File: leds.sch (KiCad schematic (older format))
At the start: 36 parts

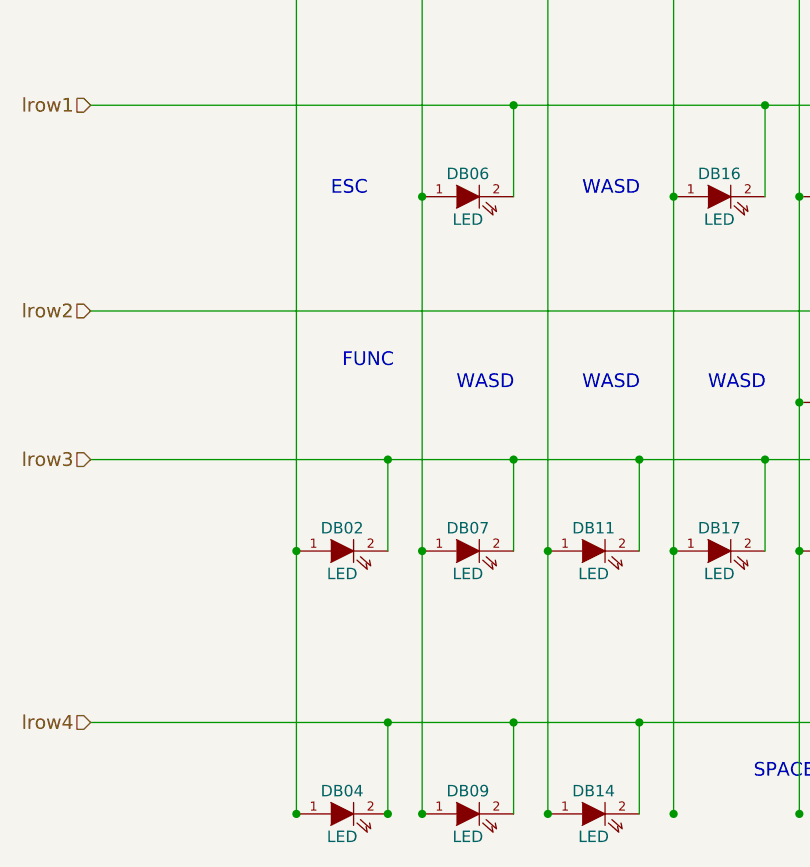
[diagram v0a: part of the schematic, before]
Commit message: Change the cyrstal footprint / correct two wrong diode directions
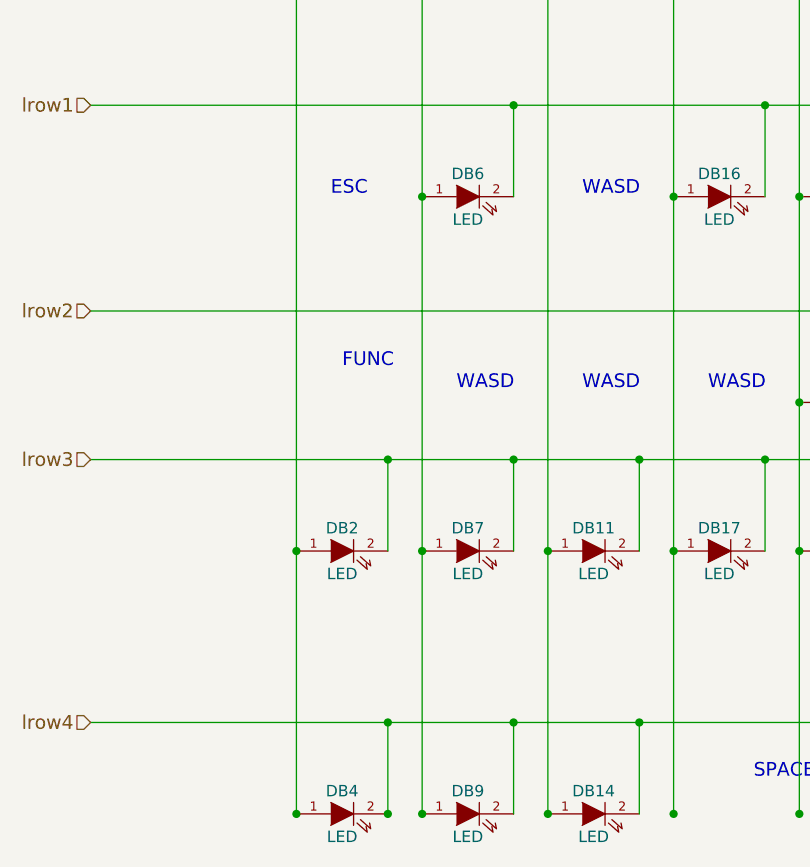
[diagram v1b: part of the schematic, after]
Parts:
- renumbered DB02 to DB2, DB04 to DB4, DB06 to DB6, DB07 to DB7, DB09 to DB9
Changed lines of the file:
@@
-EESchema Schematic File Version 2  date 11/23/2013 1:19:47 PM
+EESchema Schematic File Version 2
 LIBS:power
 LIBS:mx1a-simple
@@
 LIBS:usb_ports
 LIBS:keyboard-cache
-EELAYER 27 0
+EELAYER 25 0
 EELAYER END
 $Descr A4 11693 8268
@@
 $EndComp
 $Comp
-L LED DB06
+L LED DB6
 U 1 1 5190074C
 P 2800 1950
-F 0 "DB06" H 2800 2050 50  0000 C CNN
+F 0 "DB6" H 2800 2050 50  0000 C CNN
 F 1 "LED" H 2800 1850 50  0000 C CNN
 F 2 "" H 2800 1950 60  0001 C CNN
@@
 $EndComp
 $Comp
-L LED DB02
+L LED DB2
 U 1 1 519007B5
 P 2250 3500
-F 0 "DB02" H 2250 3600 50  0000 C CNN
+F 0 "DB2" H 2250 3600 50  0000 C CNN
 F 1 "LED" H 2250 3400 50  0000 C CNN
 F 2 "" H 2250 3500 60  0001 C CNN
@@
 $EndComp
 $Comp
-L LED DB07
+L LED DB7
 U 1 1 519007BC
 P 2800 3500
-F 0 "DB07" H 2800 3600 50  0000 C CNN
+F 0 "DB7" H 2800 3600 50  0000 C CNN
 F 1 "LED" H 2800 3400 50  0000 C CNN
 F 2 "" H 2800 3500 60  0001 C CNN
@@
 $EndComp
 $Comp
-L LED DB04
+L LED DB4
 U 1 1 51900887
 P 2250 4650
-F 0 "DB04" H 2250 4750 50  0000 C CNN
+F 0 "DB4" H 2250 4750 50  0000 C CNN
 F 1 "LED" H 2250 4550 50  0000 C CNN
 F 2 "" H 2250 4650 60  0001 C CNN
@@
 $EndComp
 $Comp
-L LED DB09
+L LED DB9
 U 1 1 5190088E
 P 2800 4650
-F 0 "DB09" H 2800 4750 50  0000 C CNN
+F 0 "DB9" H 2800 4750 50  0000 C CNN
 F 1 "LED" H 2800 4550 50  0000 C CNN
 F 2 "" H 2800 4650 60  0001 C CNN
